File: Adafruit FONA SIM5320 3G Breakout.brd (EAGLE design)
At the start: 45.7 x 49.5 mm, 60 parts, among them CN2 JSTPH, IC1 74VHCT125PW, Q2 bss138, SW1 KMR2, U1 SIM5320, U2 MCP73831T-2ACI/OT, X1 uFL, X2 MicroB, X3 uFL, X4 4UCONN_18510, X6 SIM_LOCKAMPHENOL

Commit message: 最小構成
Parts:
- removed C11: 10uF, microbuilder:0805-NO
- removed C14, C16: 33pF, microbuilder:RESPACK_4X0603
- removed C15, C17: 10pF, microbuilder:RESPACK_4X0603
- removed C4: 33pF, microbuilder:0805-NO
- removed C8: 10pF, microbuilder:0805-NO
- removed D6: 1N4148, microbuilder:SOD-323
- removed IC1: 74VHCT125PW, 74xx-us:TSSOP14
- removed Q2: bss138, microbuilder:SOT23-WIDE
- removed R6: 2K, microbuilder:0805-NO
- removed R8: 10K, microbuilder:0805-NO
- removed TP1: TPTP11R, testpad:TP11R
- removed X4: 4UCONN_18510, microbuilder:4UCONN_18510
- moved D5 5.71 mm to (21.3, 9.78)
- moved D3 0.77 mm to (17.0, 7.87)
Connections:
- removed net 2.8V: Q2.1, R6.2, TP1.TP, U1.44
- removed net DTR_5V: D6.C, JP1.9
- removed net EAR+: C11.2, C4.1, C8.1, U1.26
- removed net EAR-: U1.25
- removed net HP+: C11.1, X4.2-TIP, X4.3-OUTER_SLEEVE
- removed net MIC+: C14.1, C14.2, C15.1, C15.2, JP1.15, U1.23, X4.1-GND
- removed net MIC-: C14.3, C14.4, C14.6, C14.7, C15.3, C15.5, C15.6, C15.7, JP1.16, U1.24
- removed net NETSTAT_5V: IC1.6, JP1.14, R5.2
- removed net PWRSTAT_5V: IC1.3, JP1.13, R4.2
- removed net RI_5V: IC1.11, JP1.12
- removed net RTS_5V: JP1.10, Q2.3, R8.1
- removed net SPEAKER+: C16.1, C16.2, C17.1, C17.2, JP1.17, U1.21
- removed net SPEAKER-: C16.3, C16.4, C16.6, C16.7, C17.3, C17.5, C17.6, C17.7, JP1.18, U1.22
- removed net TXD_5V: IC1.8, JP1.7
- removed net VCCIO: IC1.14, JP1.4, R8.2
- net GND: no longer C14.5, C14.8, C15.4, C15.8, C16.5, C16.8, C17.4, C17.8, C4.2, C8.2, IC1.1, IC1.10, IC1.13, IC1.4, IC1.7, X4.4-INNER_SLEEVE
- net NETSTAT: now also JP1.14, R5.2; no longer IC1.5
- net PWRSTAT: now also JP1.13, R4.2; no longer IC1.2
- net RI: now also JP1.12; no longer IC1.12
- net UART_DTR: now also JP1.9; no longer D6.A
- net UART_RTS: now also JP1.10; no longer Q2.2
- net UART_RXD: no longer R6.1
- net UART_TXD: now also JP1.7; no longer IC1.9
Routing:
- net MIC+: track 92.8 -> 0.00 mm, vias 5 -> 0
- net 2.8V: track 68.5 -> 0.00 mm, vias 3 -> 0
- net PWRSTAT_5V: track 60.9 -> 0.00 mm, vias 2 -> 0
- net NETSTAT_5V: track 60.3 -> 0.00 mm, vias 3 -> 0
- net EAR+: track 48.7 -> 0.00 mm
- net MIC-: track 34.5 -> 0.00 mm
- net VCCIO: track 33.1 -> 0.00 mm, vias 2 -> 0
- net SPEAKER-: track 24.3 -> 0.00 mm
- net SPEAKER+: track 22.1 -> 0.00 mm
- net TXD_5V: track 15.0 -> 0.00 mm, vias 1 -> 0
- net HP+: track 13.3 -> 0.00 mm
- net UART_TXD: track 41.7 -> 29.9 mm, vias 2 -> 1
- net PWRSTAT: track 40.3 -> 49.8 mm, vias 2 -> 1
- net NETSTAT: track 39.1 -> 48.5 mm, vias 2 -> 1
- net PWRKEY: track 52.9 -> 44.1 mm
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
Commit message: 部品をPCB Fusion化
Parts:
- removed CHRG: ORANGE, microbuilder:CHIPLED_0805_NOOUTLINE
- removed DONE, PWRSTAT: GREEN, microbuilder:CHIPLED_0805_NOOUTLINE
- removed NETSTAT: RED, microbuilder:CHIPLED_0805_NOOUTLINE
- removed SW1: KMR2, microbuilder:BTN_KMR2_4.6X2.8
- removed X1: uFL, microbuilder:SMA_EDGELAUNCH_UFL
- removed X3: uFL, microbuilder:U.FL
- added ANT1, ANT2: U-FL, Seeed-Connector:U-FL3P-SMD-2.6X2.6X1.0MM
- added D6, D7, D8: 1N4148, Seeed-Diode:LL-34
- added D9: GREEN-0603, Seeed-LED:LED-0603
- added SW3: B3U-1000P-2P-SMD, Seeed-Switch:SW2-2.6-3.0X2.5X1.2+0.4MM
- C1: value 10µF -> 10uf; device microbuilder:0805-NO -> Seeed-Capacitor:C0603
- C10, C3, C6: value 33pF -> 33pf; device microbuilder:0805-NO -> Seeed-Capacitor:C0402
- C5: value 10pF -> 10pf; device microbuilder:0805-NO -> Seeed-Capacitor:C0402
- C9: value 10uF -> 10uf; device microbuilder:0805-NO -> Seeed-Capacitor:C0805
- CN2: value JSTPH -> 2P-2.0-90D-SMD; device microbuilder:JSTPH2 -> Seeed-Connector:HW2-SMD-2.0-90D
- D3: value 1N4148 -> RED-0805; device microbuilder:SOD-323 -> Seeed-LED:LED-0805
- D4: value 1N4148 -> GREEN-0603; device microbuilder:SOD-323 -> Seeed-LED:LED-0603
- D5: value 1N4148 -> YELLOW-0603; device microbuilder:SOD-323 -> Seeed-LED:LED-0603
- L2: value 33nH -> 15NH-300MA; device microbuilder:_0805MP -> Seeed-Inductor:L0402
- R1: value 470 -> 470R; device microbuilder:0805-NO -> Seeed-Resistor:R0603
- R2, R3, R4, R5: device microbuilder:0805-NO -> Seeed-Resistor:R0603
- moved D4 44.3 mm to (33.3, 46.9), turned to 270 degrees
- moved D3 41.5 mm to (29.7, 47.4), turned to 270 degrees
- moved D5 29.6 mm to (2.03, 32.3), turned to 0 degrees
- moved C3 0.63 mm to (10.5, 21.5), turned to 90 degrees
- moved L2 0.51 mm to (7.11, 21.5)
- moved C5 0.38 mm to (11.4, 41.9), turned to 90 degrees
- moved C6 0.30 mm to (11.6, 39.8), turned to 90 degrees
- moved R4 0.28 mm to (31.6, 46.9), turned to 0 degrees
- moved CN2 0.28 mm to (3.79, 39.7), turned to 270 degrees
- moved C1 0.25 mm to (7.37, 28.3), turned to 0 degrees
- moved R1 0.25 mm to (6.10, 32.3), turned to 90 degrees
- moved C10 0.25 mm to (10.4, 19.4), turned to 0 degrees
- moved R2 0.24 mm to (6.10, 34.2), turned to 90 degrees
- moved R3 0.18 mm to (10.2, 27.7), turned to 270 degrees
- moved C9 0.13 mm to (35.2, 46.9), turned to 180 degrees
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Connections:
- net +5V: now also D5.+; no longer CHRG.A
- net CTS_5V: now also D7.C; no longer D3.C
- net GND: now also ANT1.GND1, ANT1.GND2, ANT2.GND1, ANT2.GND2, CN2.-, D3.-, D4.-, D9.-, SW3.1; no longer CN2.1, DONE.C, NETSTAT.C, PWRSTAT.C, SW1.A, SW1.A', X1.GND@1, X1.GND@2, X1.GND@3, X1.GND@4, X3.1, X3.2
- net GSM_ANT: now also ANT1.D; no longer X1.P
- net N$1: now also D5.-; no longer CHRG.C
- net N$3: now also ANT2.D; no longer X3.3
- net N$4: now also D4.+; no longer PWRSTAT.A
- net N$6: now also D9.+; no longer DONE.A
- net N$9: now also D3.+; no longer NETSTAT.A
- net PWRKEY: now also D8.A, SW3.2; no longer D5.A, SW1.B, SW1.B'
- net PWRKEY_5V: now also D8.C; no longer D5.C
- net RXD_5V: now also D6.C; no longer D4.C
- net UART_CTS: now also D7.A; no longer D3.A
- net UART_RXD: now also D6.A; no longer D4.A
- net VBAT: now also CN2.+; no longer CN2.2
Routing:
- net GND: track 17.8 -> 7.91 mm, vias 47 -> 45
- net PWRKEY: track 44.1 -> 40.1 mm
- net UART_RXD: track 29.3 -> 27.6 mm
- net RXD_5V: track 3.94 -> 5.08 mm
- net N$6: track 1.73 -> 2.54 mm
- net VBAT: track 104.7 -> 105.5 mm
- net N$4: track 2.44 -> 1.65 mm
- net N$7: track 2.81 -> 3.57 mm
- net UART_CTS: track 29.1 -> 28.3 mm
- net N$1: track 2.02 -> 2.54 mm

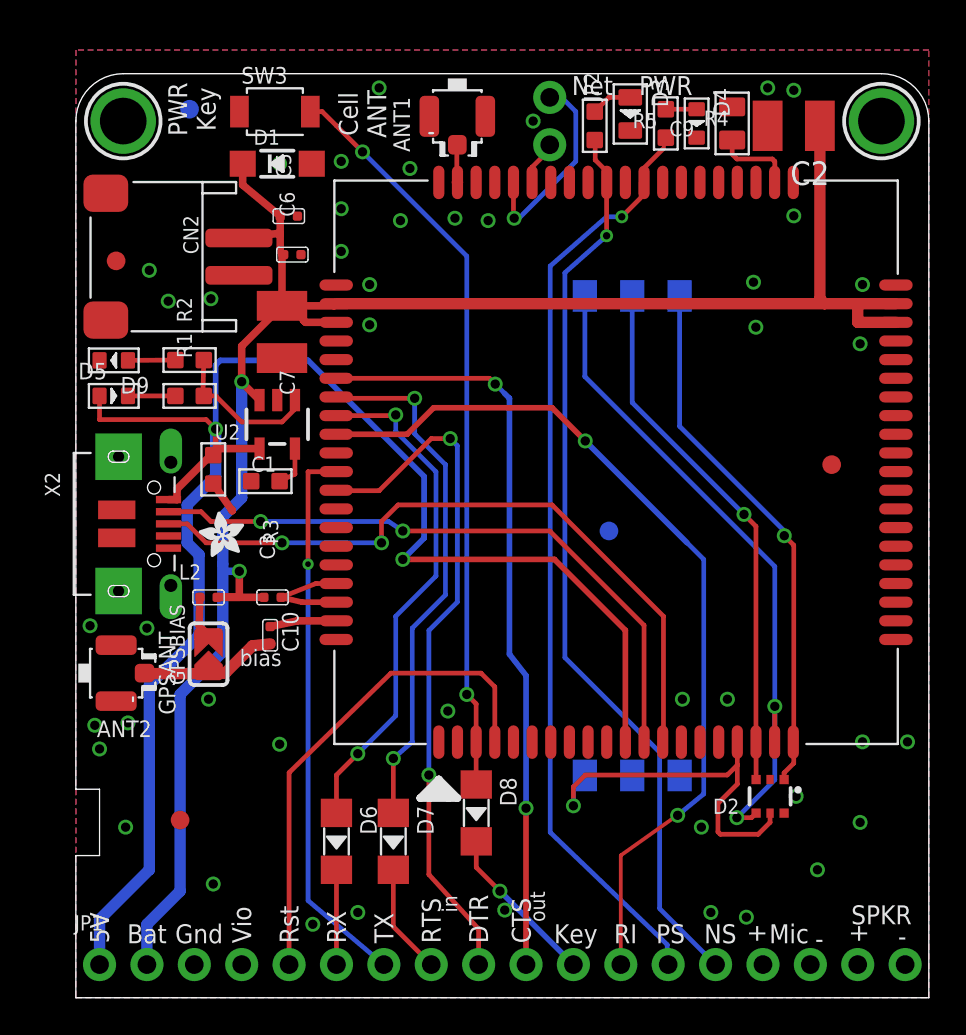
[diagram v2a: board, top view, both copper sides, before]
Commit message: USBをPCBのパーツ化
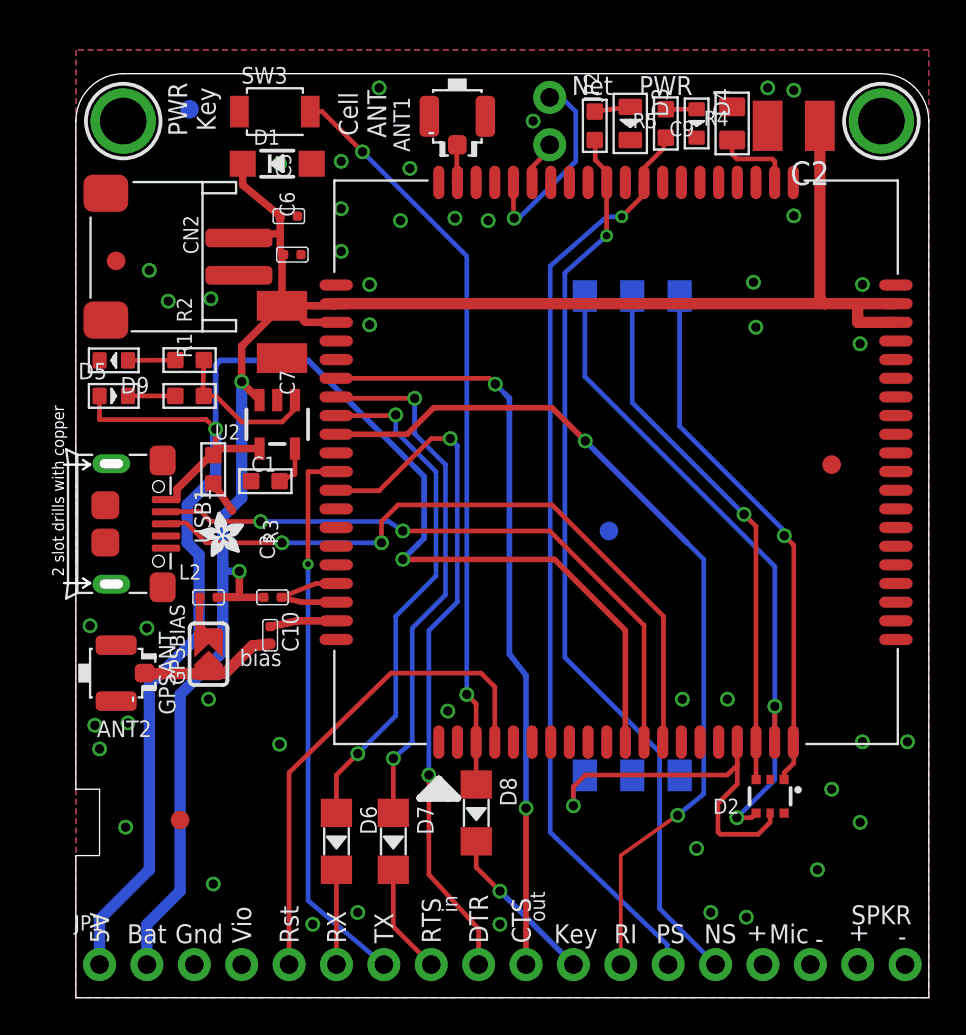
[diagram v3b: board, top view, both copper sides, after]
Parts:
- removed X2: MicroB, microbuilder:4UCONN_20329
- added USB1: ST-USB-001G, Seeed-Connector:MICRO-USB5+4P-SMD-0.65-B
- moved D3 0.51 mm to (29.7, 46.9)
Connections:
- net +5V: now also USB1.1; no longer X2.VBUS
- net DM: now also USB1.2; no longer X2.D-
- net DP: now also USB1.3; no longer X2.D+
- net GND: now also USB1.5, USB1.S1, USB1.S2, USB1.S3, USB1.S4, USB1.S5, USB1.S6; no longer X2.BASE@1, X2.BASE@2, X2.GND, X2.SPRT@1, X2.SPRT@2, X2.SPRT@3, X2.SPRT@4
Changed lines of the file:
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@@
 <attribute name="VALUE" value="2K" x="9.779" y="28.321" size="0.8128" layer="27" font="vector" ratio="10" rot="R270"/>
-</element>
-<element name="X2" library="microbuilder" package="4UCONN_20329" value="MicroB" x="4.191" y="25.4" smashed="yes" rot="R270">
-<attribute name="NAME" x="-1.661" y="28.178" size="0.8128" layer="25" ratio="18" rot="R270"/>
-<attribute name="VALUE" x="-1.965" y="27.543" size="0.8128" layer="27" font="vector" ratio="10" rot="R270"/>
 </element>
 <element name="D1" library="microbuilder" package="SOD-123" value="MMSZ5231BT1G" x="10.795" y="44.704" smashed="yes">
@@
 <attribute name="MPN" value="B3U-1000P-2P-SMD" x="10.668" y="47.498" size="1.778" layer="27" display="off"/>
 </element>
-<element name="D3" library="Seeed-LED" library_urn="urn:adsk.eagle:library:472" package="LED-0805" value="RED-0805" x="29.718" y="47.371" rot="R270">
-<attribute name="MPN" value="17-215SURC/S530-A2/TR8" x="29.718" y="47.371" size="1.778" layer="27" rot="R270" display="off"/>
+<element name="D3" library="Seeed-LED" library_urn="urn:adsk.eagle:library:472" package="LED-0805" value="RED-0805" x="29.718" y="46.863" rot="R270">
+<attribute name="MPN" value="17-215SURC/S530-A2/TR8" x="29.718" y="46.863" size="1.778" layer="27" rot="R270" display="off"/>
 </element>
 <element name="D4" library="Seeed-LED" library_urn="urn:adsk.eagle:library:472" package="LED-0603" value="GREEN-0603" x="33.274" y="46.863" rot="R270">
@@
 </element>
 <element name="ANT2" library="Seeed-Connector" library_urn="urn:adsk.eagle:library:478" package="U-FL3P-SMD-2.6X2.6X1.0MM" value="U-FL" x="2.159" y="17.399" rot="R180"/>
+<element name="USB1" library="Seeed-Connector" library_urn="urn:adsk.eagle:library:478" package="MICRO-USB5+4P-SMD-0.65-B" value="ST-USB-001G" x="5.08" y="25.4" rot="R270">
+<attribute name="MPN" value="ST-USB-001G" x="5.08" y="25.4" size="1.778" layer="27" rot="R270" display="off"/>
+</element>
 </elements>
 <signals>
 <signal name="GND">
-<contactref element="X2" pad="BASE@1"/>
-<contactref element="X2" pad="BASE@2"/>
-<contactref element="X2" pad="GND"/>
-<contactref element="X2" pad="SPRT@1"/>
-<contactref element="X2" pad="SPRT@2"/>
-<contactref element="X2" pad="SPRT@3"/>
-<contactref element="X2" pad="SPRT@4"/>
 <contactref element="C1" pad="2"/>
 <contactref element="R3" pad="2"/>
@@
 <wire x1="13.956" y1="21.202" x2="12.126" y2="21.202" width="0.3048" layer="1"/>
 <wire x1="12.126" y1="21.202" x2="11.0035" y2="21.463" width="0.3048" layer="1"/>
-<via x="38.608" y="10.795" extent="1-16" drill="0.5"/>
+<via x="40.513" y="11.176" extent="1-16" drill="0.5"/>
 <via x="39.751" y="6.858" extent="1-16" drill="0.5"/>
 <via x="42.037" y="9.398" extent="1-16" drill="0.5"/>
 <via x="34.036" y="4.572" extent="1-16" drill="0.5"/>
-<via x="22.987" y="4.699" extent="1-16" drill="0.5"/>
+<via x="22.733" y="3.937" extent="1-16" drill="0.5"/>
 <via x="15.113" y="4.572" extent="1-16" drill="0.5"/>
 <via x="12.7" y="3.937" extent="1-16" drill="0.5"/>
 <via x="7.366" y="6.096" extent="1-16" drill="0.5"/>
 <via x="35.941" y="4.318" extent="1-16" drill="0.5"/>
-<via x="33.528" y="9.144" extent="1-16" drill="0.5"/>
+<via x="33.274" y="8.001" extent="1-16" drill="0.5"/>
 <via x="32.512" y="16.002" extent="1-16" drill="0.5"/>
 <via x="34.925" y="16.002" extent="1-16" drill="0.5"/>
@@
 <contactref element="ANT2" pad="GND2"/>
 <contactref element="ANT2" pad="GND1"/>
+<contactref element="USB1" pad="5"/>
+<contactref element="USB1" pad="S6"/>
+<contactref element="USB1" pad="S4"/>
+<contactref element="USB1" pad="S5"/>
+<contactref element="USB1" pad="S3"/>
+<contactref element="USB1" pad="S2"/>
+<contactref element="USB1" pad="S1"/>
 </signal>
 <signal name="N$1">
@@
 <contactref element="R5" pad="1"/>
 <contactref element="D3" pad="+"/>
-<wire x1="27.813" y1="47.498" x2="28.575" y2="48.26" width="0.254" layer="1"/>
-<wire x1="28.575" y1="48.26" x2="29.718" y2="48.26" width="0.254" layer="1"/>
+<wire x1="27.813" y1="47.498" x2="28.702" y2="47.625" width="0.254" layer="1"/>
+<wire x1="28.702" y1="47.625" x2="29.718" y2="47.752" width="0.254" layer="1"/>
 </signal>
 <signal name="VBAT">
@@
 <contactref element="U2" pad="4"/>
 <contactref element="C1" pad="1"/>
-<contactref element="X2" pad="VBUS"/>
 <contactref element="U1" pad="11"/>
 <contactref element="JP1" pad="1"/>
-<wire x1="4.966" y1="26.7" x2="5.425" y2="26.7" width="0.4064" layer="1"/>
 <wire x1="1.27" y1="30.988" x2="6.985" y2="30.988" width="0.254" layer="1"/>
 <wire x1="6.985" y1="30.988" x2="7.493" y2="30.48" width="0.254" layer="1"/>
@@
 <contactref element="D5" pad="+"/>
 <wire x1="1.27" y1="32.258" x2="1.27" y2="30.988" width="0.254" layer="1"/>
+<contactref element="USB1" pad="1"/>
+<wire x1="5.334" y1="26.67" x2="4.8768" y2="26.67" width="0.1524" layer="1"/>
+<wire x1="4.8768" y1="26.67" x2="4.83" y2="26.7" width="0.1524" layer="1"/>
+<wire x1="5.334" y1="26.67" x2="5.425" y2="26.7" width="0.1524" layer="1"/>
 </signal>
 <signal name="RXD_5V">
@@
 <signal name="DM">
 <contactref element="U1" pad="12"/>
-<contactref element="X2" pad="D-"/>
-<wire x1="4.966" y1="26.05" x2="6.716" y2="26.05" width="0.254" layer="1"/>
 <wire x1="6.716" y1="26.05" x2="7.239" y2="25.527" width="0.254" layer="1"/>
 <wire x1="7.239" y1="25.527" x2="9.906" y2="25.527" width="0.254" layer="1"/>
@@
 <wire x1="25.4" y1="25.019" x2="30.456" y2="19.963" width="0.254" layer="1"/>
 <wire x1="30.456" y1="19.963" x2="30.456" y2="13.702" width="0.254" layer="1"/>
+<contactref element="USB1" pad="2"/>
+<wire x1="6.7056" y1="26.0604" x2="4.8768" y2="26.0604" width="0.254" layer="1"/>
+<wire x1="4.8768" y1="26.0604" x2="4.83" y2="26.05" width="0.1524" layer="1"/>
+<wire x1="6.7056" y1="26.0604" x2="6.716" y2="26.05" width="0.1524" layer="1"/>
 </signal>
 <signal name="DP">
 <contactref element="U1" pad="13"/>
-<contactref element="X2" pad="D+"/>
-<wire x1="4.966" y1="25.4" x2="5.969" y2="25.4" width="0.254" layer="1"/>
 <wire x1="5.969" y1="25.4" x2="6.985" y2="24.384" width="0.254" layer="1"/>
 <wire x1="6.985" y1="24.384" x2="11.049" y2="24.384" width="0.254" layer="1"/>
@@
 <wire x1="31.496" y1="20.447" x2="31.496" y2="13.742" width="0.254" layer="1"/>
 <wire x1="31.496" y1="13.742" x2="31.456" y2="13.702" width="0.254" layer="1"/>
+<contactref element="USB1" pad="3"/>
+<wire x1="5.9436" y1="25.4508" x2="4.8768" y2="25.4508" width="0.254" layer="1"/>
+<wire x1="4.8768" y1="25.4508" x2="4.83" y2="25.4" width="0.1524" layer="1"/>
+<wire x1="5.9436" y1="25.4508" x2="5.969" y2="25.4" width="0.1524" layer="1"/>
 </signal>
 <signal name="CTS_5V">

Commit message: 最小構成ver1.1.0
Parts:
- removed CN2: 2P-2.0-90D-SMD, Seeed-Connector:HW2-SMD-2.0-90D
- removed D5: YELLOW-0603, Seeed-LED:LED-0603
- removed D9: GREEN-0603, Seeed-LED:LED-0603
- removed FID3: FIDUCIAL"", microbuilder:FIDUCIAL_1MM
- removed R3: 2K, Seeed-Resistor:R0603
- removed U2: MCP73831T-2ACI/OT, microbuilder:SOT23-5
- added C11: 100uf, Seeed-Capacitor:AVX-B
- added C12: 1uf, Seeed-Capacitor:C0603
- added C4: 47uf, Seeed-Capacitor:AVX-B
- added C8: 100nf, Seeed-Capacitor:C0402
- added IC1: MIC29302WU, MIC29302WU:TO263-5
- C2: value 100uF -> 47uf; device rcl:C1210 -> Seeed-Capacitor:AVX-B
- C7: value 100uF -> 100uf; device rcl:C1210 -> Seeed-Capacitor:AVX-B
- R1: value 470R -> 100K
- R2: value 1K -> 47K
- moved C1 24.9 mm to (2.16, 3.94), turned to 270 degrees
- moved C7 18.3 mm to (3.05, 19.2), turned to 180 degrees
- moved USB1 16.2 mm to (5.97, 9.27)
- moved R2 11.6 mm to (2.16, 23.2)
- moved R1 11.4 mm to (2.16, 21.6), turned to 270 degrees
- moved L2 4.60 mm to (9.27, 17.4)
- moved C3 4.11 mm to (11.2, 17.4)
- moved U$25 3.30 mm to (5.59, 25.5)
- moved C10 3.14 mm to (11.2, 16.4), turned to 270 degrees
- moved ANT2 1.91 mm to (2.16, 15.5)
- moved C6 1.85 mm to (12.7, 41.4)
- moved C5 1.45 mm to (12.7, 42.7)
- moved R5 0.25 mm to (27.8, 47.0)
- moved C2 0.13 mm to (38.6, 46.7)
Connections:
- removed net N$1: D5.-, R1.1
- removed net N$5: R3.1, U2.5
- removed net N$6: D9.+, R2.1
- new net VIO: C11.+, C12.2, IC1.1, IC1.2, JP1.4
- net +5V: no longer D5.+, U2.4
- net GND: now also C11.-, C12.1, C2.-, C4.-, C7.-, C8.2, IC1.3, R2.2; no longer C2.2, C7.2, CN2.-, D9.-, R3.2, U2.2
- net N$2: now also IC1.5, R2.1; no longer R2.2, U2.1
- net VBAT: now also C2.+, C4.+, C7.+, C8.1, IC1.4, R1.1; no longer C2.1, C7.1, CN2.+, U2.3
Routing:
- net +5V: track 89.7 -> 45.2 mm
- net VIO: track 0.00 -> 29.7 mm, vias 0 -> 1
- net VBAT: track 105.5 -> 118.4 mm
- net GND: track 7.91 -> 0.00 mm, vias 45 -> 8
- net N$2: track 8.19 -> 15.8 mm
- net N$6: track 2.54 -> 0.00 mm
- net N$1: track 2.54 -> 0.00 mm
- net N$5: track 2.27 -> 0.00 mm
- net N$7: track 3.57 -> 5.67 mm
- net DM: track 34.4 -> 32.5 mm
- net DP: track 37.9 -> 36.1 mm
- net N$3: track 7.35 -> 8.14 mm
- net UART_TXD: track 29.9 -> 29.3 mm

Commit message: 修正
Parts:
- moved JP2 0.89 mm to (24.5, 47.0)
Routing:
- net I2C_SDA: track 10.9 -> 5.46 mm, vias 1 -> 0
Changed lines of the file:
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@@
 <attribute name="VALUE" value="33pf" x="11.176" y="16.383" size="1.778" layer="27" rot="R270" display="off"/>
 </element>
-<element name="JP2" library="microbuilder" package="1X02_ROUND" value="" x="25.4" y="46.99" rot="R270"/>
+<element name="JP2" library="microbuilder" package="1X02_ROUND" value="" x="24.511" y="46.99" rot="R270"/>
 <element name="U$42" library="microbuilder" package="ADAFRUIT_TEXT_20MM" value="" x="37.846" y="10.16" rot="MR90"/>
 <element name="ANT1" library="Seeed-Connector" library_urn="urn:adsk.eagle:library:478" package="U-FL3P-SMD-2.6X2.6X1.0MM" value="U-FL" x="20.447" y="47.244" rot="R90"/>
@@
 <via x="32.512" y="16.002" extent="1-16" drill="0.5"/>
 <via x="34.925" y="16.002" extent="1-16" drill="0.5"/>
-<via x="24.511" y="46.99" extent="1-16" drill="0.5"/>
 <via x="38.481" y="48.641" extent="1-16" drill="0.5"/>
 <via x="37.084" y="48.768" extent="1-16" drill="0.5"/>
@@
 <contactref element="U1" pad="56"/>
 <contactref element="JP2" pad="1"/>
-<wire x1="25.4" y1="48.26" x2="26.035" y2="48.26" width="0.254" layer="16"/>
-<wire x1="26.035" y1="48.26" x2="26.797" y2="47.498" width="0.254" layer="16"/>
-<wire x1="26.797" y1="47.498" x2="26.797" y2="44.831" width="0.254" layer="16"/>
-<wire x1="26.797" y1="44.831" x2="23.749" y2="41.783" width="0.254" layer="16"/>
-<wire x1="23.749" y1="41.783" x2="23.495" y2="41.783" width="0.254" layer="16"/>
-<via x="23.495" y="41.783" extent="1-16" drill="0.5"/>
-<wire x1="23.495" y1="41.783" x2="23.456" y2="41.822" width="0.254" layer="1"/>
-<wire x1="23.456" y1="41.822" x2="23.456" y2="43.702" width="0.254" layer="1"/>
+<wire x1="24.511" y1="48.26" x2="24.257" y2="48.26" width="0.4064" layer="1"/>
+<wire x1="24.257" y1="48.26" x2="23.114" y2="47.117" width="0.4064" layer="1"/>
+<wire x1="23.114" y1="47.117" x2="23.114" y2="44.704" width="0.4064" layer="1"/>
+<wire x1="23.114" y1="44.704" x2="23.495" y2="44.323" width="0.4064" layer="1"/>
+<wire x1="23.495" y1="44.323" x2="23.495" y2="43.741" width="0.4064" layer="1"/>
+<wire x1="23.495" y1="43.741" x2="23.456" y2="43.702" width="0.4064" layer="1"/>
 </signal>
 <signal name="I2C_SCL">
 <contactref element="U1" pad="55"/>
 <contactref element="JP2" pad="2"/>
-<wire x1="24.456" y1="43.702" x2="24.456" y2="44.522" width="0.254" layer="1"/>
-<wire x1="24.456" y1="44.522" x2="25.4" y2="45.466" width="0.254" layer="1"/>
-<wire x1="25.4" y1="45.466" x2="25.4" y2="45.72" width="0.254" layer="1"/>
+<wire x1="24.511" y1="45.72" x2="24.511" y2="43.757" width="0.4064" layer="1"/>
+<wire x1="24.511" y1="43.757" x2="24.456" y2="43.702" width="0.4064" layer="1"/>
 </signal>
 <signal name="N$2">
